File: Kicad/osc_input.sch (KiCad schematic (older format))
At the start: 20 parts, among them Q1 BC547b, Q2 BC547b, U1 LM2931A, U2 CONN_01X04, U3 CONN_01X03

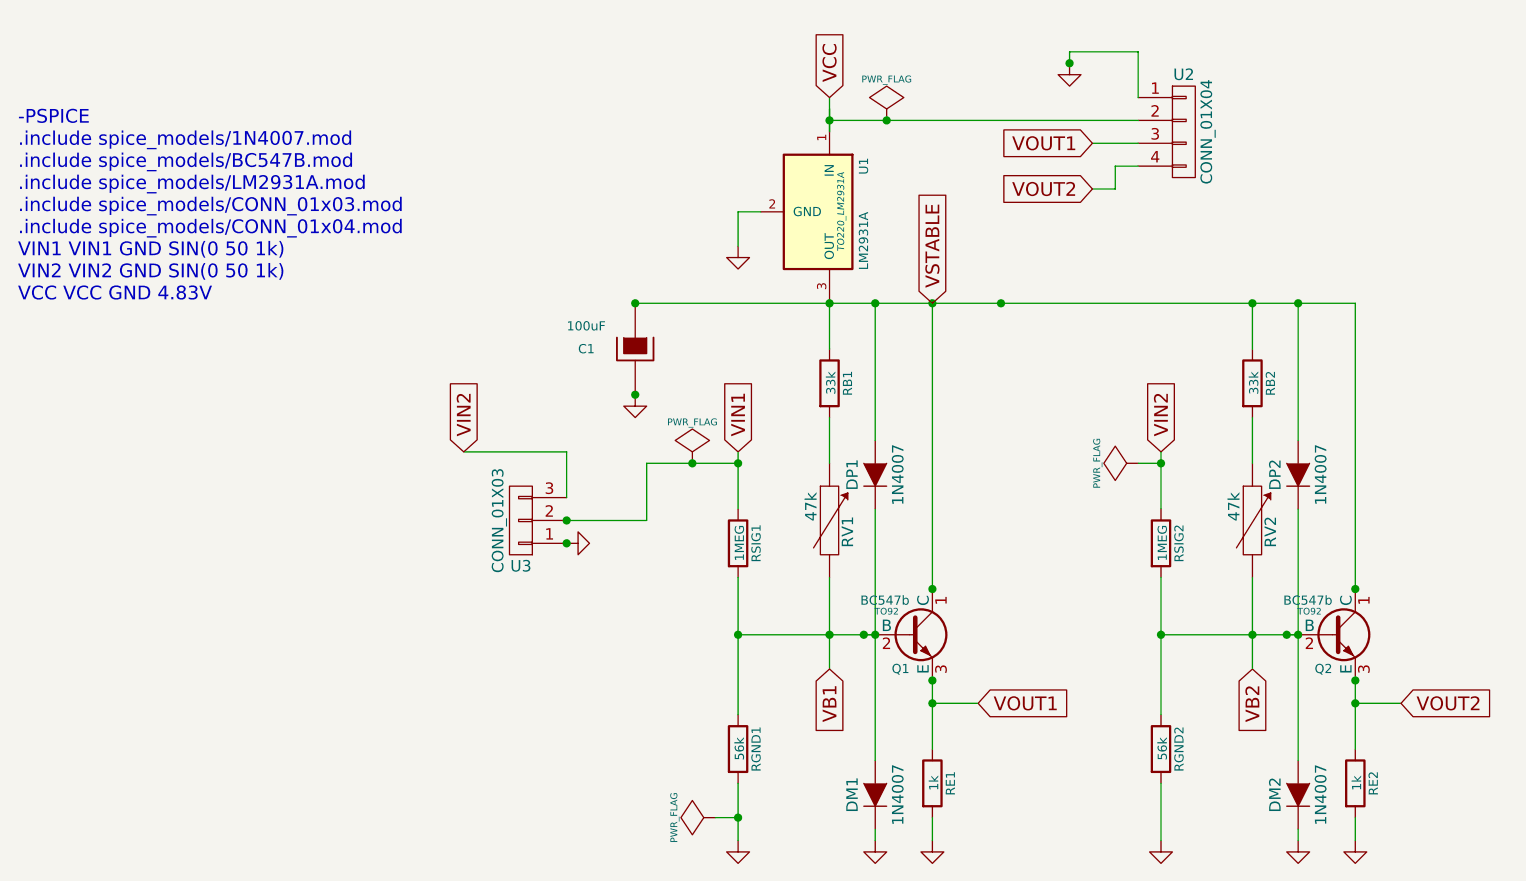
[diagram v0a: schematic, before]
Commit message: Kicad: Updated to fit kicad version 4.0.4. Modified routing for next prototype.
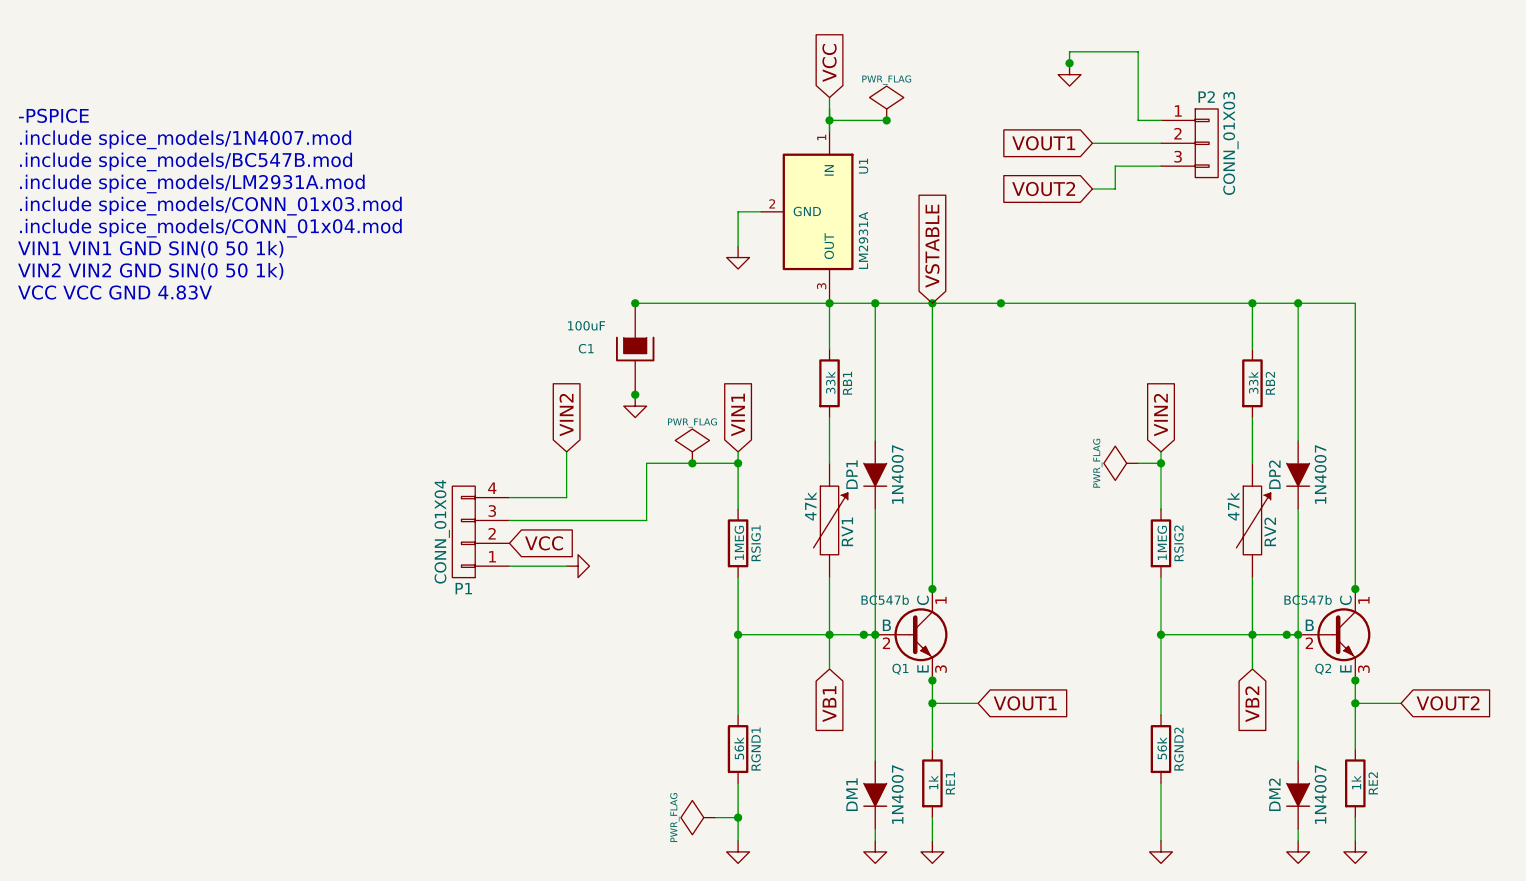
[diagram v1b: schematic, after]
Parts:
- removed U2: CONN_01X04, symbol CONN_01X04
- removed U3: CONN_01X03, symbol CONN_01X03
- added P1: CONN_01X04, boul51:PinHeader_x4, symbol CONN_01X04
- added P2: CONN_01X03, boul51:PinHeader_x3, symbol CONN_01X03
- C1: footprint ~ -> Capacitors_THT:C_Radial_D10_L20_P5
- DM1, DM2, DP1, DP2: footprint (none) -> boul51:Diode-DO41
- Q1: footprint TO92 -> boul51:TO-92_1
- Q2: footprint TO92 -> boul51:TO-92_2
- RB1, RB2, RE1, RE2, RGND1, RGND2, RSIG1, RSIG2: footprint ~ -> Resistors_THT:Resistor_Horizontal_RM10mm
- RV1, RV2: footprint ~ -> boul51:Pot_5x8mm
- U1: footprint TO220_LM2931A -> TO_SOT_Packages_THT:TO-220_Neutral123_Vertical
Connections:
- wire segments 48 -> 50
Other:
- note added: "-PSPICE \n.include spice_models/1N4007.mod\n.include spice_models/BC547B.mod\n.include spice_models/LM2931A.mod\n.include spice_models/CONN_01x03.mod\n.include spice_models/CONN_01x04.mod\nVIN1 VIN1 GND SIN(0 50 1k)\nVIN2 VIN2 GND SIN(0 50 1k)\nVCC VCC GND 4.83V\n"
- note removed: "-PSPICE \n.include spice_models/1N4007.mod\n.include spice_models/BC547B.mod\n.include spice_models/LM2931A.mod\n.include spice_models/CONN_01x03.mod\n.include spice_models/CONN_01x04.mod\nVIN1 VIN1 GND SIN(0 50 1k)\nVIN2 VIN2 GND SIN(0 50 1k)\nVCC VCC GND 4.83V"
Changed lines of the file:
@@
 LIBS:contrib
 LIBS:valves
-LIBS:components_sch
 LIBS:osc_input-cache
 EELAYER 25 0
@@
 F 0 "RB1" V 4380 3350 40  0000 C CNN
 F 1 "33k" V 4307 3351 40  0000 C CNN
-F 2 "~" V 4230 3350 30  0000 C CNN
+F 2 "Resistors_THT:Resistor_Horizontal_RM10mm" V 4230 3350 30  0001 C CNN
 F 3 "~" H 4300 3350 30  0000 C CNN
 	1    4300 3350
@@
 F 0 "C1" H 3200 3200 40  0000 L CNN
 F 1 "100uF" H 3150 3300 40  0000 L CNN
-F 2 "~" H 3550 3050 30  0000 C CNN
+F 2 "Capacitors_THT:C_Radial_D10_L20_P5" H 3550 3050 30  0001 C CNN
 F 3 "~" H 3450 3200 300 0000 C CNN
 	1    3450 3200
@@
 F 0 "Q1" H 4650 4301 40  0000 R CNN
 F 1 "BC547b" H 4650 4600 40  0000 R CNN
-F 2 "TO92" H 4550 4552 29  0000 C CNN
+F 2 "boul51:TO-92_1" H 4550 4552 29  0001 C CNN
 F 3 "" H 4650 4450 60  0000 C CNN
 	1    4650 4450
@@
 F 0 "RE1" V 4830 5100 40  0000 C CNN
 F 1 "1k" V 4757 5101 40  0000 C CNN
-F 2 "~" V 4680 5100 30  0000 C CNN
+F 2 "Resistors_THT:Resistor_Horizontal_RM10mm" V 4680 5100 30  0001 C CNN
 F 3 "~" H 4750 5100 30  0000 C CNN
 	1    4750 5100
@@
 F 0 "RSIG1" V 3980 4050 40  0000 C CNN
 F 1 "1MEG" V 3907 4051 40  0000 C CNN
-F 2 "~" V 3830 4050 30  0000 C CNN
+F 2 "Resistors_THT:Resistor_Horizontal_RM10mm" V 3830 4050 30  0001 C CNN
 F 3 "~" H 3900 4050 30  0000 C CNN
 	1    3900 4050
@@
 F 0 "RGND1" V 3980 4950 40  0000 C CNN
 F 1 "56k" V 3907 4951 40  0000 C CNN
-F 2 "~" V 3830 4950 30  0000 C CNN
+F 2 "Resistors_THT:Resistor_Horizontal_RM10mm" V 3830 4950 30  0001 C CNN
 F 3 "~" H 3900 4950 30  0000 C CNN
 	1    3900 4950
@@
 	4300 2200 4300 2100
 Text Notes 750  3000 0    60   ~ 0
--PSPICE \n.include spice_models/1N4007.mod\n.include spice_models/BC547B.mod\n.include spice_models/LM2931A.mod\n.include spice_models/CONN_01x03.mod\n.include spice_models/CONN_01x04.mod\nVIN1 VIN1 GND SIN(0 50 1k)\nVIN2 VIN2 GND SIN(0 50 1k)\nVCC VCC GND 4.83V
+-PSPICE \n.include spice_models/1N4007.mod\n.include spice_models/BC547B.mod\n.include spice_models/LM2931A.mod\n.include spice_models/CONN_01x03.mod\n.include spice_models/CONN_01x04.mod\nVIN1 VIN1 GND SIN(0 50 1k)\nVIN2 VIN2 GND SIN(0 50 1k)\nVCC VCC GND 4.83V\n
 Text GLabel 4300 4600 3    60   Input ~ 0
 VB1
@@
 F 0 "RV1" V 4380 3900 50  0000 C CNN
 F 1 "47k" V 4220 4010 50  0000 C CNN
-F 2 "~" H 4300 3950 60  0000 C CNN
+F 2 "boul51:Pot_5x8mm" H 4300 3950 60  0001 C CNN
 F 3 "~" H 4300 3950 60  0000 C CNN
 	1    4300 3950
@@
 Wire Wire Line
 	4300 3500 4300 3700
-Wire Wire Line
-	4300 2200 5650 2200
 Connection ~ 4550 2200
 Connection ~ 4300 2200
@@
 F 0 "U1" H 4050 2800 40  0000 C CNN
 F 1 "LM2931A" H 4250 2800 40  0000 L CNN
-F 2 "TO220_LM2931A" H 4250 2700 30  0000 C CIN
+F 2 "TO_SOT_Packages_THT:TO-220_Neutral123_Vertical" H 4250 2700 30  0001 C CIN
 F 3 "" H 4250 2600 60  0000 C CNN
 	1    4250 2600
@@
 F 0 "RB2" V 6230 3350 40  0000 C CNN
 F 1 "33k" V 6157 3351 40  0000 C CNN
-F 2 "~" V 6080 3350 30  0000 C CNN
+F 2 "Resistors_THT:Resistor_Horizontal_RM10mm" V 6080 3350 30  0001 C CNN
 F 3 "~" H 6150 3350 30  0000 C CNN
 	1    6150 3350
@@
 F 0 "Q2" H 6500 4301 40  0000 R CNN
 F 1 "BC547b" H 6500 4600 40  0000 R CNN
-F 2 "TO92" H 6400 4552 29  0000 C CNN
+F 2 "boul51:TO-92_2" H 6400 4552 29  0001 C CNN
 F 3 "" H 6500 4450 60  0000 C CNN
 	1    6500 4450
@@
 F 0 "RE2" V 6680 5100 40  0000 C CNN
 F 1 "1k" V 6607 5101 40  0000 C CNN
-F 2 "~" V 6530 5100 30  0000 C CNN
+F 2 "Resistors_THT:Resistor_Horizontal_RM10mm" V 6530 5100 30  0001 C CNN
 F 3 "~" H 6600 5100 30  0000 C CNN
 	1    6600 5100
@@
 F 0 "RSIG2" V 5830 4050 40  0000 C CNN
 F 1 "1MEG" V 5757 4051 40  0000 C CNN
-F 2 "~" V 5680 4050 30  0000 C CNN
+F 2 "Resistors_THT:Resistor_Horizontal_RM10mm" V 5680 4050 30  0001 C CNN
 F 3 "~" H 5750 4050 30  0000 C CNN
 	1    5750 4050
@@
 F 0 "RGND2" V 5830 4950 40  0000 C CNN
 F 1 "56k" V 5757 4951 40  0000 C CNN
-F 2 "~" V 5680 4950 30  0000 C CNN
+F 2 "Resistors_THT:Resistor_Horizontal_RM10mm" V 5680 4950 30  0001 C CNN
 F 3 "~" H 5750 4950 30  0000 C CNN
 	1    5750 4950
@@
 F 0 "RV2" V 6230 3900 50  0000 C CNN
 F 1 "47k" V 6070 4010 50  0000 C CNN
-F 2 "~" H 6150 3950 60  0000 C CNN
+F 2 "boul51:Pot_5x8mm" H 6150 3950 60  0001 C CNN
 F 3 "~" H 6150 3950 60  0000 C CNN
 	1    6150 3950
@@
 L GND #PWR013
 U 1 1 5524F834
-P 3150 4050
-F 0 "#PWR013" H 3150 4050 30  0001 C CNN
-F 1 "GND" H 3150 3980 30  0001 C CNN
-F 2 "" H 3150 4050 60  0000 C CNN
-F 3 "" H 3150 4050 60  0000 C CNN
-	1    3150 4050
-	0    -1   -1   0
-$EndComp
-Connection ~ 3150 4050
-Wire Wire Line
-	3150 3950 3500 3950
+P 3150 4150
+F 0 "#PWR013" H 3150 4150 30  0001 C CNN
+F 1 "GND" H 3150 4080 30  0001 C CNN
+F 2 "" H 3150 4150 60  0000 C CNN
+F 3 "" H 3150 4150 60  0000 C CNN
+	1    3150 4150
+	0    -1   -1   0
+$EndComp
+Wire Wire Line
+	2900 3950 3500 3950
 Wire Wire Line
 	3500 3950 3500 3700
 Connection ~ 3700 3700
-Connection ~ 3150 3950
 Wire Wire Line
 	3150 3850 3150 3650
-Wire Wire Line
-	3150 3650 2700 3650
-Text GLabel 2700 3650 1    60   Input ~ 0
+Text GLabel 3150 3650 1    60   Input ~ 0
 VIN2
 Wire Wire Line
-	5650 2100 5650 1900
+	5650 1900 5650 2200
 Wire Wire Line
 	5650 1900 5350 1900
@@
 Connection ~ 5350 1950
 Wire Wire Line
-	5650 2300 5450 2300
+	5450 2300 5750 2300
 Text GLabel 5450 2300 0    60   Input ~ 0
 VOUT1
 Wire Wire Line
-	5650 2400 5550 2400
+	5550 2400 5750 2400
 Wire Wire Line
 	5550 2400 5550 2500
@@
 F 0 "DP2" H 6350 3850 50  0000 C CNN
 F 1 "1N4007" H 6350 3650 50  0000 C CNN
-F 2 "" H 6350 3750 60  0000 C CNN
+F 2 "boul51:Diode-DO41" H 6350 3750 60  0001 C CNN
 F 3 "" H 6350 3750 60  0000 C CNN
 	1    6350 3750
@@
 F 0 "DM2" H 6350 5250 50  0000 C CNN
 F 1 "1N4007" H 6350 5050 50  0000 C CNN
-F 2 "" H 6350 5150 60  0000 C CNN
+F 2 "boul51:Diode-DO41" H 6350 5150 60  0001 C CNN
 F 3 "" H 6350 5150 60  0000 C CNN
 	1    6350 5150
@@
 F 0 "DP1" H 4500 3850 50  0000 C CNN
 F 1 "1N4007" H 4500 3650 50  0000 C CNN
-F 2 "" H 4500 3750 60  0000 C CNN
+F 2 "boul51:Diode-DO41" H 4500 3750 60  0001 C CNN
 F 3 "" H 4500 3750 60  0000 C CNN
 	1    4500 3750
@@
 F 0 "DM1" H 4500 5250 50  0000 C CNN
 F 1 "1N4007" H 4500 5050 50  0000 C CNN
-F 2 "" H 4500 5150 60  0000 C CNN
+F 2 "boul51:Diode-DO41" H 4500 5150 60  0001 C CNN
 F 3 "" H 4500 5150 60  0000 C CNN
 	1    4500 5150
@@
 Wire Wire Line
 	4500 5300 4500 5350
-$Comp
-L CONN_01X04 U2
-U 1 1 567ED7E1
-P 5850 2250
-F 0 "U2" H 5850 2500 50  0000 C CNN
-F 1 "CONN_01X04" V 5950 2250 50  0000 C CNN
-F 2 "" H 5850 2250 60  0000 C CNN
-F 3 "" H 5850 2250 60  0000 C CNN
-	1    5850 2250
-	1    0    0    -1
-$EndComp
-$Comp
-L CONN_01X03 U3
-U 1 1 567ED991
-P 2950 3950
-F 0 "U3" H 2950 4150 50  0000 C CNN
-F 1 "CONN_01X03" V 3050 3950 50  0000 C CNN
-F 2 "" H 2950 3950 60  0000 C CNN
-F 3 "" H 2950 3950 60  0000 C CNN
-	1    2950 3950
-	-1   0    0    1
-$EndComp
 Wire Wire Line
 	4750 5250 4750 5350
@@
 	5750 5350 5750 5100
 Connection ~ 6300 4450
+$Comp
+L CONN_01X04 P1
+U 1 1 584EB11D
+P 2700 4000
+F 0 "P1" H 2700 4250 50  0000 C CNN
+F 1 "CONN_01X04" V 2800 4000 50  0000 C CNN
+F 2 "boul51:PinHeader_x4" H 2700 4000 50  0001 C CNN
+F 3 "" H 2700 4000 50  0000 C CNN
+	1    2700 4000
+	-1   0    0    1
+$EndComp
+Wire Wire Line
+	2900 4150 3150 4150
+Wire Wire Line
+	2900 3850 3150 3850
+Text GLabel 2900 4050 2    60   Input ~ 0
+VCC
+$Comp
+L CONN_01X03 P2
+U 1 1 584EB8CD
+P 5950 2300
+F 0 "P2" H 5950 2500 50  0000 C CNN
+F 1 "CONN_01X03" V 6050 2300 50  0000 C CNN
+F 2 "boul51:PinHeader_x3" H 5950 2300 50  0001 C CNN
+F 3 "" H 5950 2300 50  0000 C CNN
+	1    5950 2300
+	1    0    0    -1
+$EndComp
+Wire Wire Line
+	4300 2200 4550 2200
+Wire Wire Line
+	5650 2200 5750 2200
 $EndSCHEMATC

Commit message: Kicad: Added gitignore Updated text properties in pcb Use lib from boul51.lib (removed components_sch.lib)
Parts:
- C1: symbol CAPAPOL -> CP
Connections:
- wire segments 50 -> 52
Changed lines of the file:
@@
 LIBS:contrib
 LIBS:valves
-LIBS:osc_input-cache
+LIBS:boul51
 EELAYER 25 0
 EELAYER END
@@
 $EndComp
 $Comp
-L CAPAPOL C1
+L CP C1
 U 1 1 5521821E
 P 3450 3200
@@
 Wire Wire Line
 	5650 2200 5750 2200
+Wire Wire Line
+	3450 3050 3450 3000
+Wire Wire Line
+	3450 3350 3450 3400
 $EndSCHEMATC
